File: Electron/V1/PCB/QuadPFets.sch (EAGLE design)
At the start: 53 parts, among them Q1 BC817-40SMD, Q2 BC817-40SMD, Q3 BC817-40SMD, Q4 BC817-40SMD, U1 MOSFET-PCHANNEL-SOIC8SOIC8, U2 MOSFET-PCHANNEL-SOIC8SOIC8, U3 MOSFET-PCHANNEL-SOIC8SOIC8, U4 MOSFET-PCHANNEL-SOIC8SOIC8, U5 ELECTRONDUALNAMED

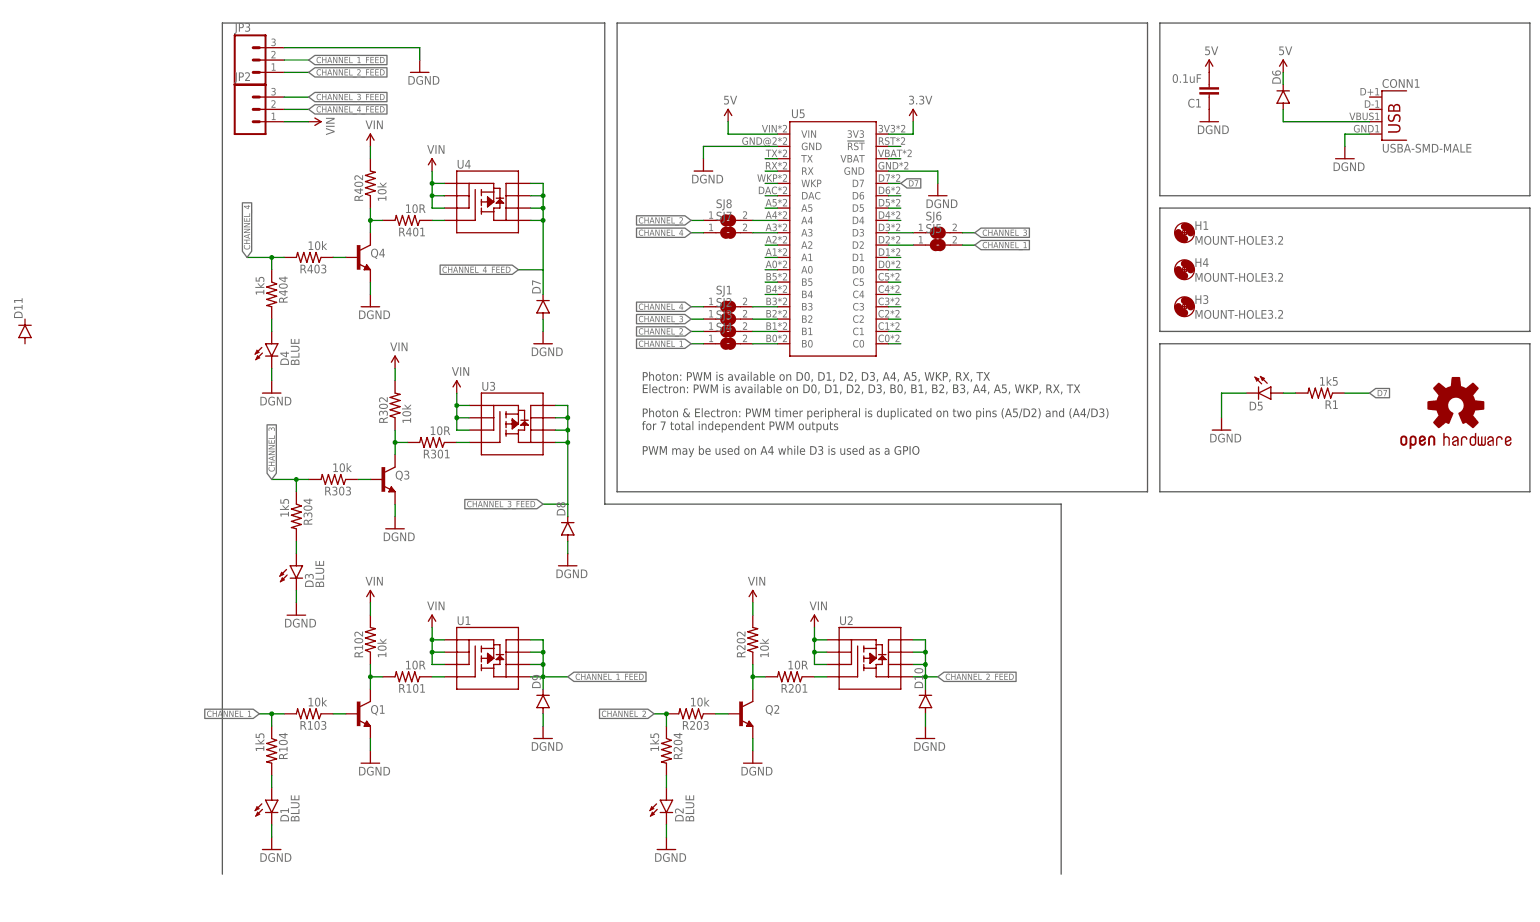
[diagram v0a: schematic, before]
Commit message: Moved LEDs to the top of the PCB so that components can be shifted left and make space between the FETs and the terminal block so that the channel id's can be shown next to the appropriate connection.
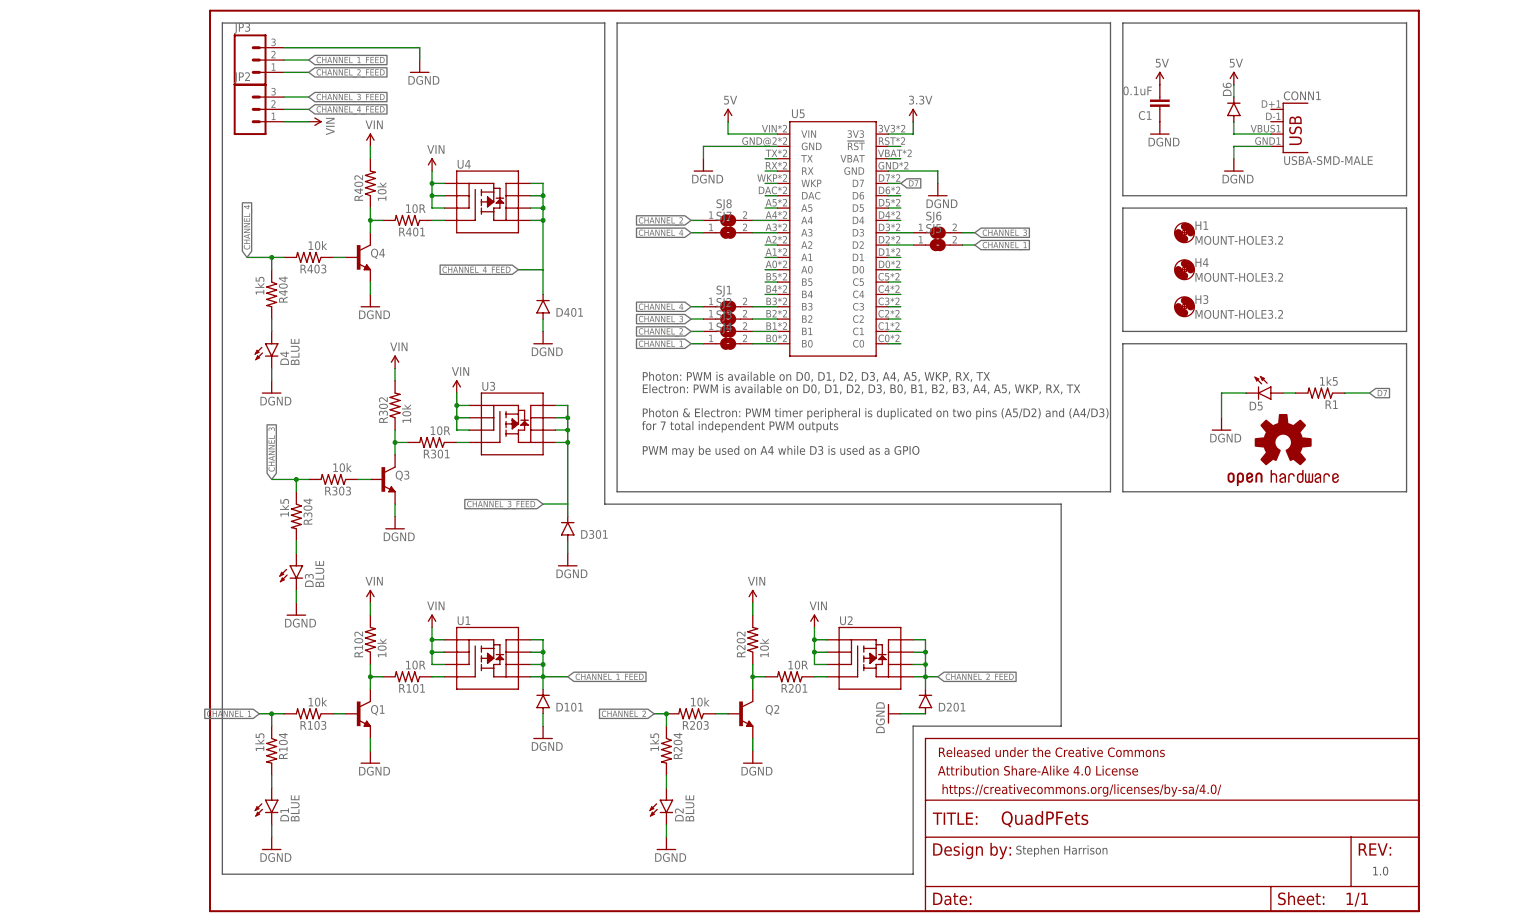
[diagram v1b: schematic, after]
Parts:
- removed D11: (no value), SparkFun-DiscreteSemi:DIODESOD123
- added FRAME2: FRAME-LETTER, SparkFun-Aesthetics:FRAME-LETTER
- renumbered D10 to D201, D7 to D401, D8 to D301, D9 to D101
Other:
- note added: "1.0"
- note added: "Stephen Harrison"
- moved on the sheet: C1, CONN1, D6
